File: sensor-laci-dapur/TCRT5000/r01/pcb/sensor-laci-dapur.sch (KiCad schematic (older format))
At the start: 5 parts

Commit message: Sensor Laci Dapur TCRT5000L rev01b
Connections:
- net +5V: now reaches Port1.1 (GND), R3.1, Sensor1.1 (CT)
- net GND: now reaches Port1.2 (+5V), R1.2, Sensor1.3 (C)
- net Out: now reaches Port1.3 (OUTPUT), R2.1
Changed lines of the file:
@@
 	0    1    1    0
-$EndComp
-$Comp
-L 1_Out Port1
-U 1 1 57893FCB
-P 5400 2700
-F 0 "Port1" H 5500 2450 60  0000 C CNN
-F 1 "1_Out" H 5500 2850 60  0000 C CNN
-F 2 "Connectors_Molex:Molex_KK-6410-03_03x2.54mm_Straight" H 5400 2700 60  0001 C CNN
-F 3 "" H 5400 2700 60  0000 C CNN
-	1    5400 2700
-	1    0    0    -1
 $EndComp
 Wire Wire Line
@@
 	3100 2200 3250 2200
 Connection ~ 4850 2200
+$Comp
+L 1_Out Port1
+U 1 1 57893FCB
+P 5400 2700
+F 0 "Port1" H 5500 2450 60  0000 C CNN
+F 1 "1_Out" H 5500 2850 60  0000 C CNN
+F 2 "Connectors_Molex:Molex_KK-6410-03_03x2.54mm_Straight" H 5400 2700 60  0001 C CNN
+F 3 "" H 5400 2700 60  0000 C CNN
+	1    5400 2700
+	1    0    0    -1
+$EndComp
+Text Label 4950 2650 0    60   ~ 0
++5V
+Text Label 4950 2750 0    60   ~ 0
+GND
+Text Label 4950 3050 0    60   ~ 0
+Out
 $EndSCHEMATC

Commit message: Change connector to JST-XH Angled
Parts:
- Port1: footprint Connectors_Molex:Molex_KK-6410-03_03x2.54mm_Straight -> Connectors_JST:JST_XH_S03B-XH-A_03x2.50mm_Angled
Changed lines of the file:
@@
 F 0 "Port1" H 5500 2450 60  0000 C CNN
 F 1 "1_Out" H 5500 2850 60  0000 C CNN
-F 2 "Connectors_Molex:Molex_KK-6410-03_03x2.54mm_Straight" H 5400 2700 60  0001 C CNN
+F 2 "Connectors_JST:JST_XH_S03B-XH-A_03x2.50mm_Angled" H 5400 2700 60  0001 C CNN
 F 3 "" H 5400 2700 60  0000 C CNN
 	1    5400 2700

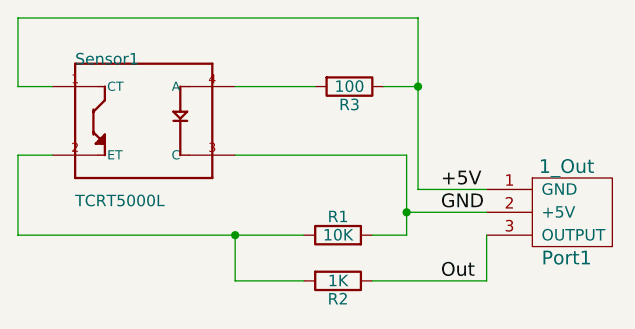
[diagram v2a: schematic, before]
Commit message: Adjust pin order and component locations
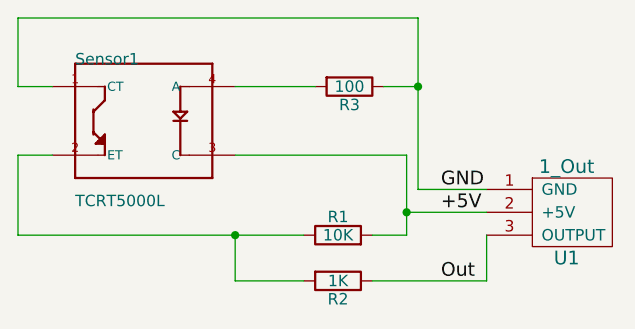
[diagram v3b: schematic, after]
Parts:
- removed Port1: 1_Out, Connectors_JST:JST_XH_S03B-XH-A_03x2.50mm_Angled, symbol 1_Out
- added U1: 1_Out, Connectors_JST:JST_XH_S03B-XH-A_03x2.50mm_Angled, symbol 1_Out
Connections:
- net +5V: now also R1.2, Sensor1.3 (C), U1.2 (+5V); no longer R3.1, Sensor1.1 (CT)
- net GND: now also R3.1, Sensor1.1 (CT), U1.1 (GND); no longer R1.2, Sensor1.3 (C)
- net Out: now also U1.3 (OUTPUT)
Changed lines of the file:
@@
 	5150 3050 4650 3050
 Wire Wire Line
-	5150 2750 4800 2750
+	4800 2750 5150 2750
 Wire Wire Line
 	4800 2500 4800 2850
@@
 	3100 2200 3250 2200
 Connection ~ 4850 2200
+Text Label 4950 2750 0    60   ~ 0
++5V
+Text Label 4950 2650 0    60   ~ 0
+GND
+Text Label 4950 3050 0    60   ~ 0
+Out
 $Comp
-L 1_Out Port1
-U 1 1 57893FCB
+L 1_Out U1
+U 1 1 57A009A5
 P 5400 2700
-F 0 "Port1" H 5500 2450 60  0000 C CNN
+F 0 "U1" H 5500 2450 60  0000 C CNN
 F 1 "1_Out" H 5500 2850 60  0000 C CNN
 F 2 "Connectors_JST:JST_XH_S03B-XH-A_03x2.50mm_Angled" H 5400 2700 60  0001 C CNN
@@
 	1    0    0    -1
 $EndComp
-Text Label 4950 2650 0    60   ~ 0
-+5V
-Text Label 4950 2750 0    60   ~ 0
-GND
-Text Label 4950 3050 0    60   ~ 0
-Out
 $EndSCHEMATC
